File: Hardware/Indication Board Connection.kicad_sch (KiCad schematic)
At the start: 14 parts, among them J18 Conn_01x03, U11 TPS5405DR

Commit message: added fuse, made kiCad Sharepoint a submodule, added a pulldown, added test-points
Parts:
- added TP1: TestPoint, UTSVT_Special:TestPoint_HEX_3mmID, symbol Connector:TestPoint
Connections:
- net +5V_BUCK: now also TP1.1
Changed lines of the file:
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@@
 	)
 	(junction
+		(at 66.04 137.16)
+		(diameter 0)
+		(color 0 0 0 0)
+	)
+	(junction
 		(at 182.88 69.85)
 		(diameter 0)
@@
 	(wire
 		(pts
-			(xy 66.04 134.62) (xy 66.04 139.7)
+			(xy 66.04 134.62) (xy 66.04 137.16)
 		)
 		(stroke
@@
 	(wire
 		(pts
+			(xy 66.04 137.16) (xy 66.04 139.7)
+		)
+		(stroke
+			(width 0)
+			(type default)
+		)
+	)
+	(wire
+		(pts
 			(xy 138.43 64.77) (xy 138.43 69.85)
 		)
@@
 					(unit 1)
 				)
+			)
+		)
+	)
+	(symbol
+		(lib_id "Connector:TestPoint")
+		(at 66.04 137.16 90)
+		(unit 1)
+		(exclude_from_sim no)
+		(in_bom yes)
+		(on_board yes)
+		(dnp no)
+		(property "Reference" "TP1"
+			(at 55.88 138.684 90)
+			(effects
+				(font
+					(size 1.27 1.27)
+				)
+			)
+		)
+		(property "Value" "TestPoint"
+			(at 55.626 136.144 90)
+			(effects
+				(font
+					(size 1.27 1.27)
+				)
+			)
+		)
+		(property "Footprint" "UTSVT_Special:TestPoint_HEX_3mmID"
+			(at 66.04 132.08 0)
+			(effects
+				(font
+					(size 1.27 1.27)
+				)
+				(hide yes)
+			)
+		)
+		(property "Datasheet" "~"
+			(at 66.04 132.08 0)
+			(effects
+				(font
+					(size 1.27 1.27)
+				)
+				(hide yes)
+			)
+		)
+		(property "Description" "test point"
+			(at 66.04 137.16 0)
+			(effects
+				(font
+					(size 1.27 1.27)
+				)
+				(hide yes)
+			)
+		)
+		(pin "1"
+		)
+		(instances
+			(project "BPS-Leader"
+				(path "/fb37da34-e420-4994-8cc1-079e8c0fa48e/e5707b84-df8b-4b8b-b215-90bb9859c3b3"
+					(reference "TP1")
+					(unit 1)
+				)

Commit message: Very, very intial layout designed. Many issues. Too bad!
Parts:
- added F2: Fuse, symbol Device:Fuse
- J18: footprint (none) -> Connector_Molex:Molex_Nano-Fit_105309-xx03_1x03_P2.50mm_Vertical
- TP1: footprint UTSVT_Special:TestPoint_HEX_3mmID -> TestPoint:TestPoint_Pad_1.0x1.0mm
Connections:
- net +5V_BUCK: now also F2.1; no longer J18.1 (Pin_1)
- new net: F2.2, J18.1 (Pin_1)
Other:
- moved on the sheet: TP1
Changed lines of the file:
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@@
 	)
 	(junction
-		(at 171.45 69.85)
+		(at 59.69 137.16)
 		(diameter 0)
 		(color 0 0 0 0)
 	)
 	(junction
-		(at 66.04 137.16)
+		(at 171.45 69.85)
 		(diameter 0)
 		(color 0 0 0 0)
@@
 	(wire
 		(pts
-			(xy 66.04 134.62) (xy 66.04 137.16)
-		)
-		(stroke
-			(width 0)
-			(type default)
-		)
-	)
-	(wire
-		(pts
 			(xy 171.45 82.55) (xy 182.88 82.55)
 		)
@@
 	(wire
 		(pts
+			(xy 71.12 139.7) (xy 72.39 139.7)
+		)
+		(stroke
+			(width 0)
+			(type default)
+		)
+	)
+	(wire
+		(pts
 			(xy 171.45 69.85) (xy 171.45 72.39)
 		)
@@
 	(wire
 		(pts
+			(xy 59.69 139.7) (xy 63.5 139.7)
+		)
+		(stroke
+			(width 0)
+			(type default)
+		)
+	)
+	(wire
+		(pts
 			(xy 63.5 59.69) (xy 73.66 59.69)
 		)
@@
 	(wire
 		(pts
-			(xy 66.04 139.7) (xy 72.39 139.7)
+			(xy 128.27 64.77) (xy 138.43 64.77)
 		)
 		(stroke
@@
 	(wire
 		(pts
-			(xy 128.27 64.77) (xy 138.43 64.77)
+			(xy 86.36 64.77) (xy 87.63 64.77)
 		)
 		(stroke
@@
 	(wire
 		(pts
-			(xy 86.36 64.77) (xy 87.63 64.77)
+			(xy 59.69 134.62) (xy 59.69 137.16)
 		)
 		(stroke
@@
 	(wire
 		(pts
-			(xy 171.45 69.85) (xy 160.02 69.85)
+			(xy 59.69 137.16) (xy 59.69 139.7)
 		)
 		(stroke
@@
 	(wire
 		(pts
-			(xy 66.04 137.16) (xy 66.04 139.7)
+			(xy 171.45 69.85) (xy 160.02 69.85)
 		)
 		(stroke
@@
 	)
 	(symbol
+		(lib_id "Device:Fuse")
+		(at 67.31 139.7 90)
+		(unit 1)
+		(exclude_from_sim no)
+		(in_bom yes)
+		(on_board yes)
+		(dnp no)
+		(fields_autoplaced yes)
+		(property "Reference" "F2"
+			(at 67.31 133.35 90)
+			(effects
+				(font
+					(size 1.27 1.27)
+				)
+			)
+		)
+		(property "Value" "Fuse"
+			(at 67.31 135.89 90)
+			(effects
+				(font
+					(size 1.27 1.27)
+				)
+			)
+		)
+		(property "Footprint" ""
+			(at 67.31 141.478 90)
+			(effects
+				(font
+					(size 1.27 1.27)
+				)
+				(hide yes)
+			)
+		)
+		(property "Datasheet" "~"
+			(at 67.31 139.7 0)
+			(effects
+				(font
+					(size 1.27 1.27)
+				)
+				(hide yes)
+			)
+		)
+		(property "Description" "Fuse"
+			(at 67.31 139.7 0)
+			(effects
+				(font
+					(size 1.27 1.27)
+				)
+				(hide yes)
+			)
+		)
+		(pin "2"
+		)
+		(pin "1"
+		)
+		(instances
+			(project ""
+				(path "/fb37da34-e420-4994-8cc1-079e8c0fa48e/e5707b84-df8b-4b8b-b215-90bb9859c3b3"
+					(reference "F2")
+					(unit 1)
+				)
+			)
+		)
+	)
+	(symbol
 		(lib_id "power:GND")
 		(at 142.24 83.82 0)
@@
 	(symbol
 		(lib_id "power:+24V")
-		(at 66.04 134.62 0)
+		(at 59.69 134.62 0)
 		(unit 1)
 		(exclude_from_sim no)
@@
 		(dnp no)
 		(property "Reference" "#PWR0131"
-			(at 66.04 138.43 0)
+			(at 59.69 138.43 0)
 			(effects
 				(font
@@
 		)
 		(property "Value" "+5V_BUCK"
-			(at 65.786 130.81 0)
+			(at 59.436 130.81 0)
 			(effects
 				(font
@@
 		)
 		(property "Footprint" ""
-			(at 66.04 134.62 0)
+			(at 59.69 134.62 0)
 			(effects
 				(font
@@
 		)
 		(property "Datasheet" ""
-			(at 66.04 134.62 0)
+			(at 59.69 134.62 0)
 			(effects
 				(font
@@
 		)
 		(property "Description" "Power symbol creates a global label with name \"+24V\""
-			(at 66.04 134.62 0)
+			(at 59.69 134.62 0)
 			(effects
 				(font
@@
 	(symbol
 		(lib_id "Connector:TestPoint")
-		(at 66.04 137.16 90)
+		(at 59.69 137.16 90)
 		(unit 1)
 		(exclude_from_sim no)
@@
 		(dnp no)
 		(property "Reference" "TP1"
-			(at 55.88 138.684 90)
+			(at 49.53 138.684 90)
 			(effects
 				(font
@@
 		)
 		(property "Value" "TestPoint"
-			(at 55.626 136.144 90)
+			(at 49.276 136.144 90)
 			(effects
 				(font
@@
 			)
 		)
-		(property "Footprint" "UTSVT_Special:TestPoint_HEX_3mmID"
-			(at 66.04 132.08 0)
+		(property "Footprint" "TestPoint:TestPoint_Pad_1.0x1.0mm"
+			(at 59.69 132.08 0)
 			(effects
 				(font
@@
 		)
 		(property "Datasheet" "~"
-			(at 66.04 132.08 0)
+			(at 59.69 132.08 0)
 			(effects
 				(font
@@
 		)
 		(property "Description" "test point"
-			(at 66.04 137.16 0)
+			(at 59.69 137.16 0)
 			(effects
 				(font
@@
 			)
 		)
-		(property "Footprint" ""
+		(property "Footprint" "Connector_Molex:Molex_Nano-Fit_105309-xx03_1x03_P2.50mm_Vertical"
 			(at 77.47 142.24 0)
 			(effects

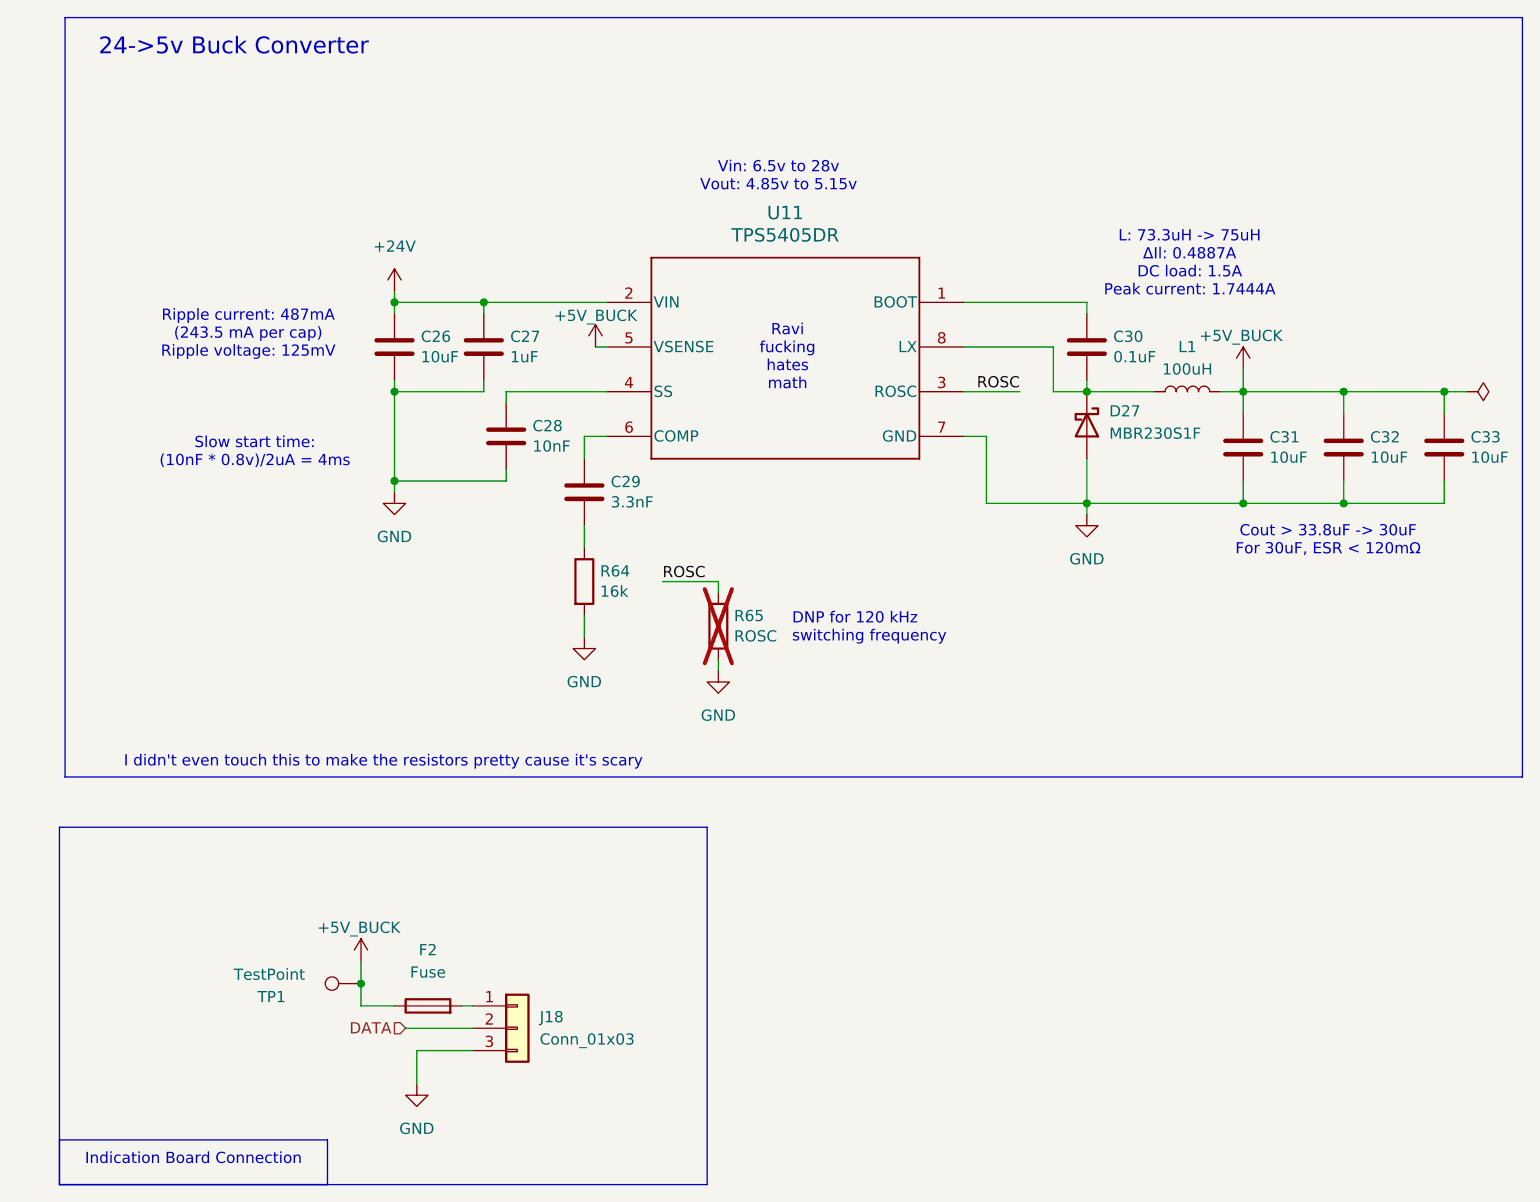
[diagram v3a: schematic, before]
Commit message: Fixed DRC violations, added missing PTC Fuse
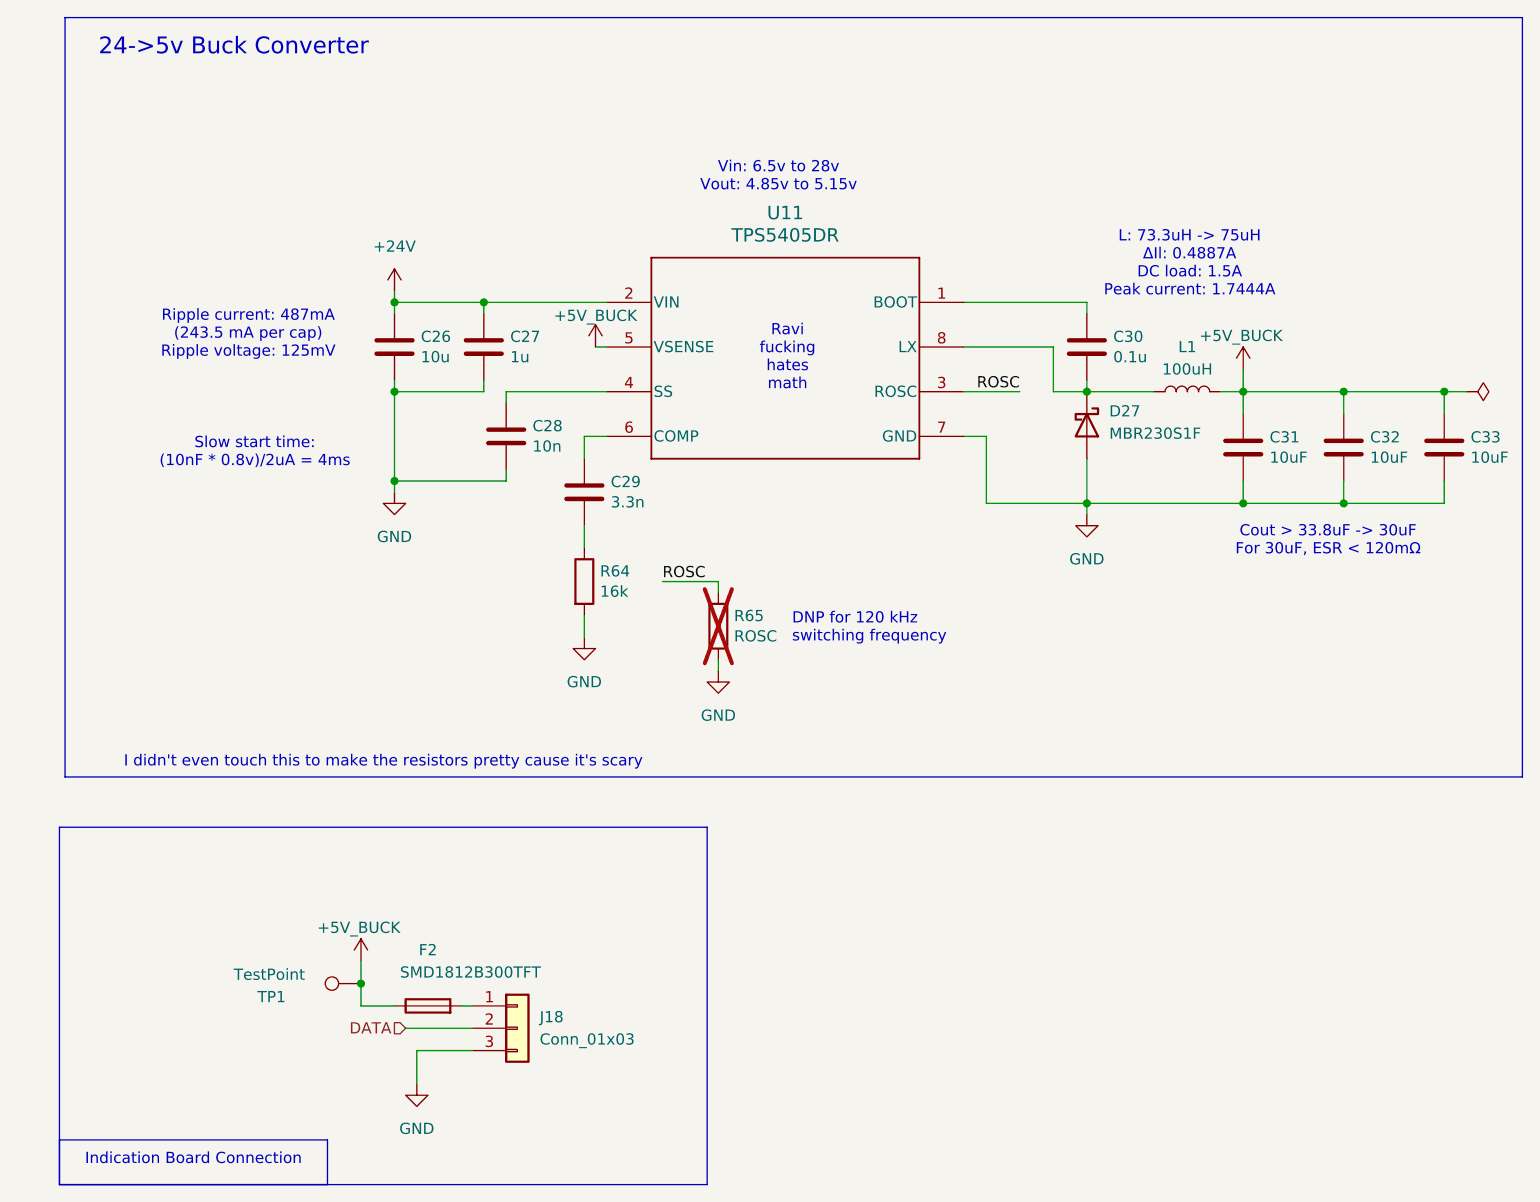
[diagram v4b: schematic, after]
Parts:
- C26: value 10uF -> 10u
- C27: value 1uF -> 1u
- C28: value 10nF -> 10n
- C29: value 3.3nF -> 3.3n
- C30: value 0.1uF -> 0.1u
- F2: value Fuse -> SMD1812B300TFT; footprint (none) -> Fuse:Fuse_1812_4532Metric
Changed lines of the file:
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@@
+			)
+		)
+		(property "Manufactuerer" ""
+			(at 85.09 91.44 0)
+			(effects
+				(font
+					(size 1.27 1.27)
+				)
+				(hide yes)
 			)
 		)
@@
 			)
 		)
-		(property "Value" "1uF"
+		(property "Value" "1u"
 			(at 76.6572 65.913 0)
 			(effects
@@
 			)
 		)
+		(property "Manufactuerer" ""
+			(at 73.66 64.77 0)
+			(effects
+				(font
+					(size 1.27 1.27)
+				)
+				(hide yes)
+			)
+		)
 		(pin "1"
 		)
@@
 			)
 		)
-		(property "Value" "3.3nF"
+		(property "Value" "3.3n"
 			(at 88.0872 82.423 0)
 			(effects
@@
 			)
 		)
+		(property "Manufactuerer" ""
+			(at 85.09 81.28 0)
+			(effects
+				(font
+					(size 1.27 1.27)
+				)
+				(hide yes)
+			)
+		)
 		(pin "1"
 		)
@@
 			)
 		)
+		(property "Manufactuerer" ""
+			(at 171.45 76.2 0)
+			(effects
+				(font
+					(size 1.27 1.27)
+				)
+				(hide yes)
+			)
+		)
 		(pin "1"
 		)
@@
 		)
 		(property "P/N" "GRM21BR61H106KE43K"
+			(at 182.88 76.2 0)
+			(effects
+				(font
+					(size 1.27 1.27)
+				)
+				(hide yes)
+			)
+		)
+		(property "Manufactuerer" ""
 			(at 182.88 76.2 0)
 			(effects
@@
 			)
 		)
+		(property "Manufactuerer" ""
+			(at 100.33 96.52 0)
+			(effects
+				(font
+					(size 1.27 1.27)
+				)
+				(hide yes)
+			)
+		)
 		(pin "1"
 		)
@@
 			)
 		)
+		(property "Manufactuerer" ""
+			(at 153.67 69.85 90)
+			(effects
+				(font
+					(size 1.27 1.27)
+				)
+				(hide yes)
+			)
+		)
 		(pin "2"
 		)
@@
 		(on_board yes)
 		(dnp no)
-		(fields_autoplaced yes)
 		(property "Reference" "F2"
 			(at 67.31 133.35 90)
@@
 			)
 		)
-		(property "Value" "Fuse"
-			(at 67.31 135.89 90)
-			(effects
-				(font
-					(size 1.27 1.27)
-				)
-			)
-		)
-		(property "Footprint" ""
+		(property "Value" "SMD1812B300TFT"
+			(at 72.136 135.89 90)
+			(effects
+				(font
+					(size 1.27 1.27)
+				)
+			)
+		)
+		(property "Footprint" "Fuse:Fuse_1812_4532Metric"
 			(at 67.31 141.478 90)
 			(effects
@@
 			)
 		)
-		(property "Datasheet" "~"
+		(property "Datasheet" "https://4donline.ihs.com/images/VipMasterIC/IC/YAGO/YAGO-S-A0012927858/YAGO-S-A0012927859-1.pdf?hkey=CECEF36DEECDED6468708AAF2E19C0C6"
 			(at 67.31 139.7 0)
 			(effects
@@
 			)
 		)
-		(property "Description" "Fuse"
+		(property "Description" "PPTC Fuse"
 			(at 67.31 139.7 0)
+			(effects
+				(font
+					(size 1.27 1.27)
+				)
+				(hide yes)
+			)
+		)
+		(property "Manufactuerer" ""
+			(at 67.31 139.7 90)
 			(effects
 				(font
@@
 			)
 		)
-		(property "Value" "0.1uF"
+		(property "Value" "0.1u"
 			(at 145.2372 65.913 0)
 			(effects
@@
 			)
 		)
+		(property "Manufactuerer" ""
+			(at 142.24 64.77 0)
+			(effects
+				(font
+					(size 1.27 1.27)
+				)
+				(hide yes)
+			)
+		)
 		(pin "1"
 		)
@@
 			)
 		)
-		(property "Value" "10uF"
+		(property "Value" "10u"
 			(at 66.4972 65.913 0)
 			(effects
@@
 		)
 		(property "P/N" "GRM21BR61H106KE43K"
+			(at 63.5 64.77 0)
+			(effects
+				(font
+					(size 1.27 1.27)
+				)
+				(hide yes)
+			)
+		)
+		(property "Manufactuerer" ""
 			(at 63.5 64.77 0)
 			(effects
@@
 			)
 		)
+		(property "Manufactuerer" ""
+			(at 160.02 76.2 0)
+			(effects
+				(font
+					(size 1.27 1.27)
+				)
+				(hide yes)
+			)
+		)
 		(pin "1"
 		)
@@
 			)
 		)
+		(property "Manufactuerer" ""
+			(at 59.69 137.16 90)
+			(effects
+				(font
+					(size 1.27 1.27)
+				)
+				(hide yes)
+			)
+		)
 		(pin "1"
 		)
@@
 			)
 		)
-		(property "Value" "10nF"
+		(property "Value" "10n"
 			(at 79.1972 76.073 0)
 			(effects
@@
 		)
 		(property "P/N" "MSASH168SB5103KTNA01"
+			(at 76.2 74.93 0)
+			(effects
+				(font
+					(size 1.27 1.27)
+				)
+				(hide yes)
+			)
+		)
+		(property "Manufactuerer" ""
 			(at 76.2 74.93 0)
 			(effects
@@
 			)
 		)
+		(property "Manufactuerer" ""
+			(at 142.24 73.66 90)
+			(effects
+				(font
+					(size 1.27 1.27)
+				)
+				(hide yes)
+			)
+		)
 		(pin "2"
 		)
@@
 			)
 		)
+		(property "Manufactuerer" ""
+			(at 77.47 142.24 0)
+			(effects
+				(font
+					(size 1.27 1.27)
+				)
+				(hide yes)
+			)
+		)
 		(pin "2"
 		)
@@
 			(at 87.63 59.69 0)
 			(effects
+				(font
+					(size 1.27 1.27)
+				)
+				(hide yes)
+			)
+		)
+		(property "Manufactuerer" ""
+			(at 87.63 59.69 0)
+			(effects
